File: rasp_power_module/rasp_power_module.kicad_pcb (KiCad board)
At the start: 2 copper layers, 45.7 x 59.3 mm, 22 parts, among them J1 Conn_01x02, J2 Conn_01x05, J3 Conn_01x02, J5 Conn_01x02, J7 Conn_01x02, J8 Conn_01x02, J9 Conn_01x02, K1 G5V-1, K2 FINDER-36.11, Q1 S8050 J3Y

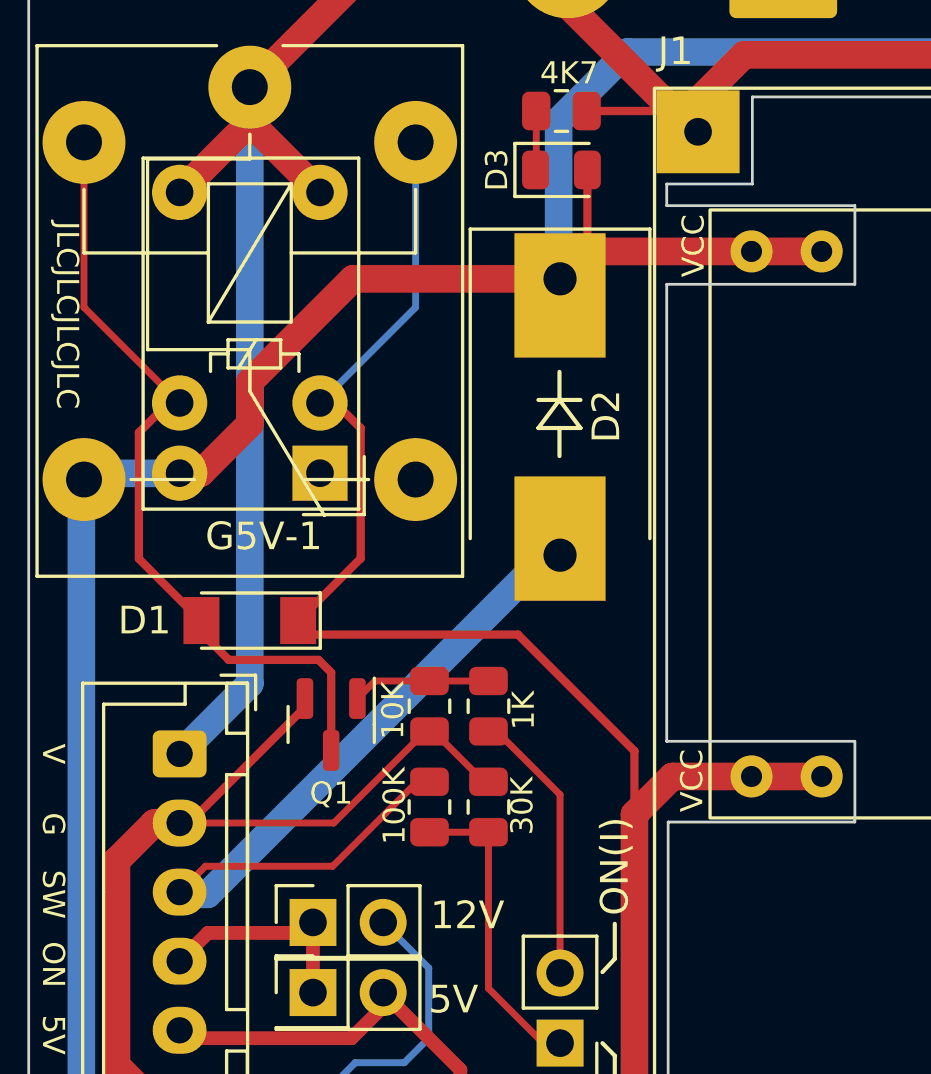
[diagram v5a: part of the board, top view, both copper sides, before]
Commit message: rasp_pm 다이오드 부품 교체
Signed-off-by: Ju, Gyeong-min <jcmh74@gmail.com>
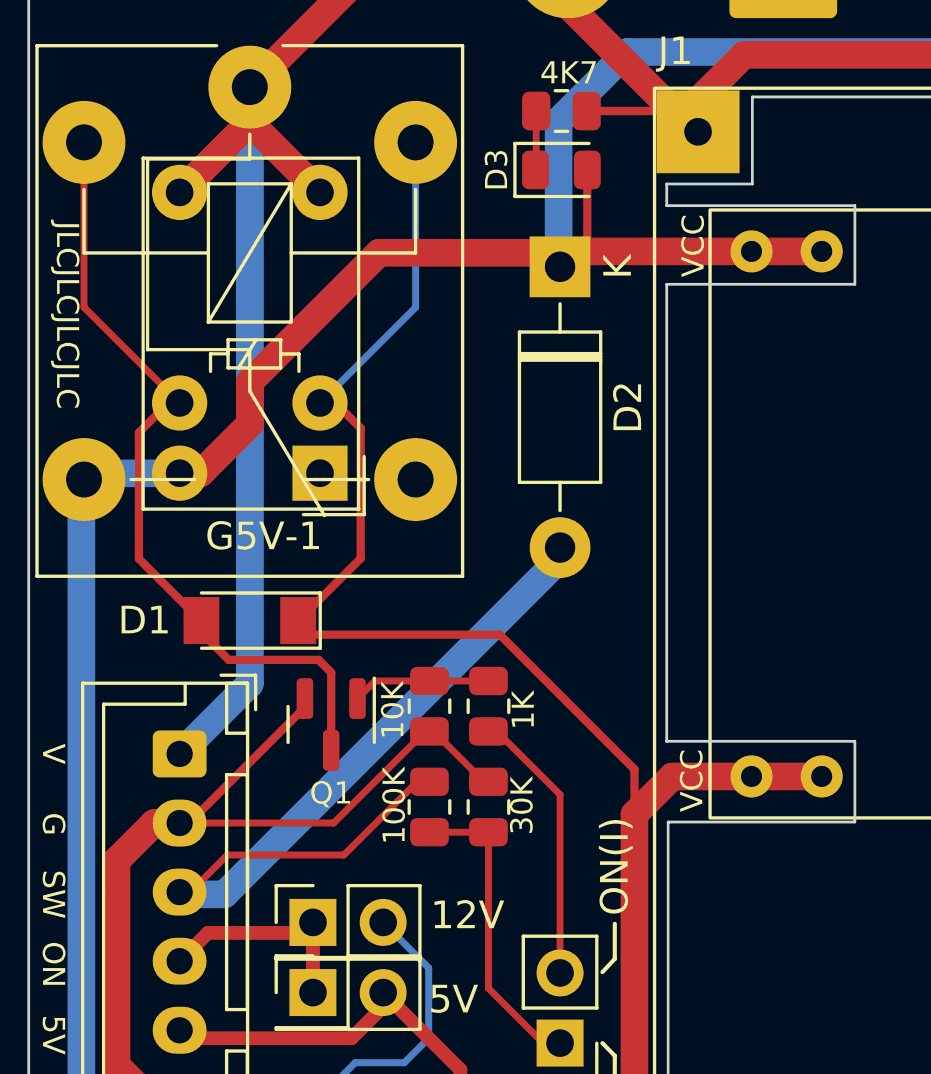
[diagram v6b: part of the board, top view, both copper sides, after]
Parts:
- D1: value ZMM5V6-M -> LL4148
- D2: value 1N4001 -> 1N4007; footprint Diode_SMD:D_SMC-RM10_Universal_Handsoldering -> Diode_THT:D_DO-41_SOD81_P10.16mm_Horizontal
- moved D2 5.44 mm to (141.0, 72.5)
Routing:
- net /SWITCH: track 29.8 -> 30.4 mm

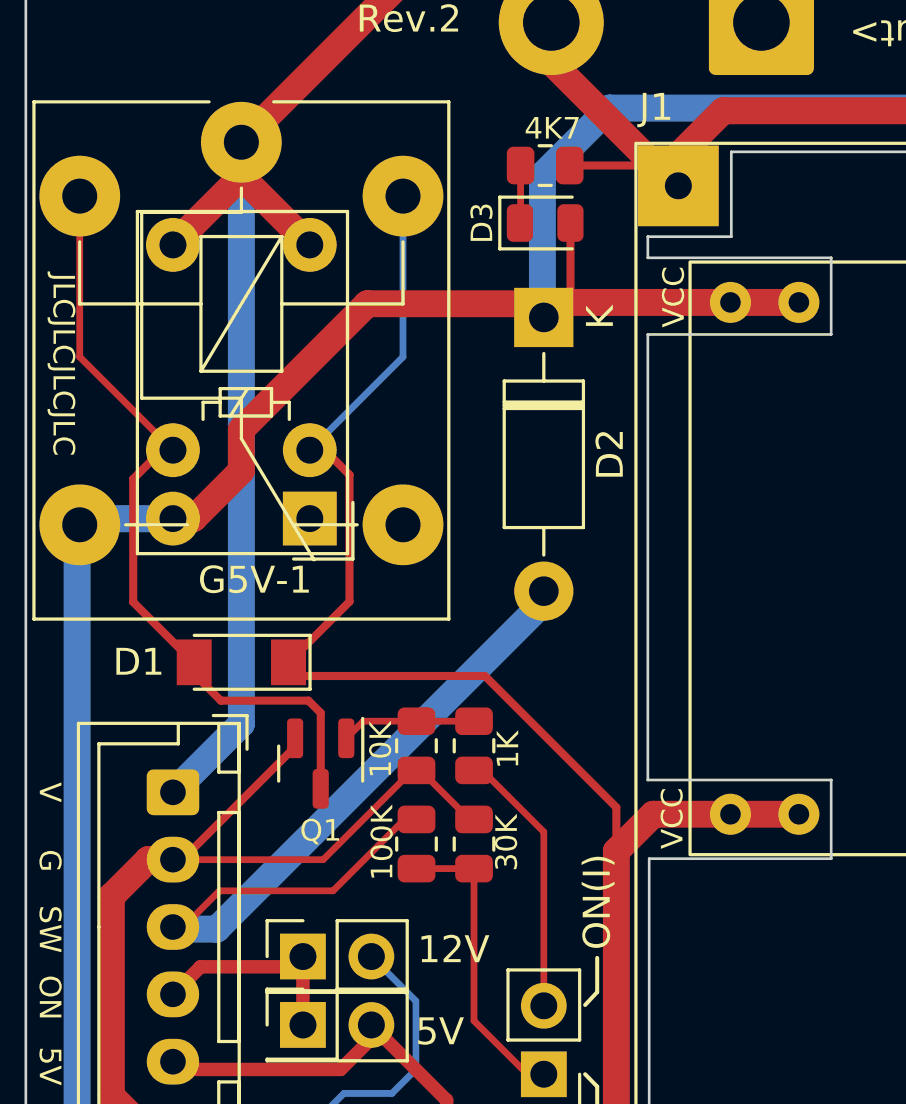
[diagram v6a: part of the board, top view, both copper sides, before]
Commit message: rasp_pi 다이오드 교체
Signed-off-by: Ju, Gyeong-min <jcmh74@gmail.com>
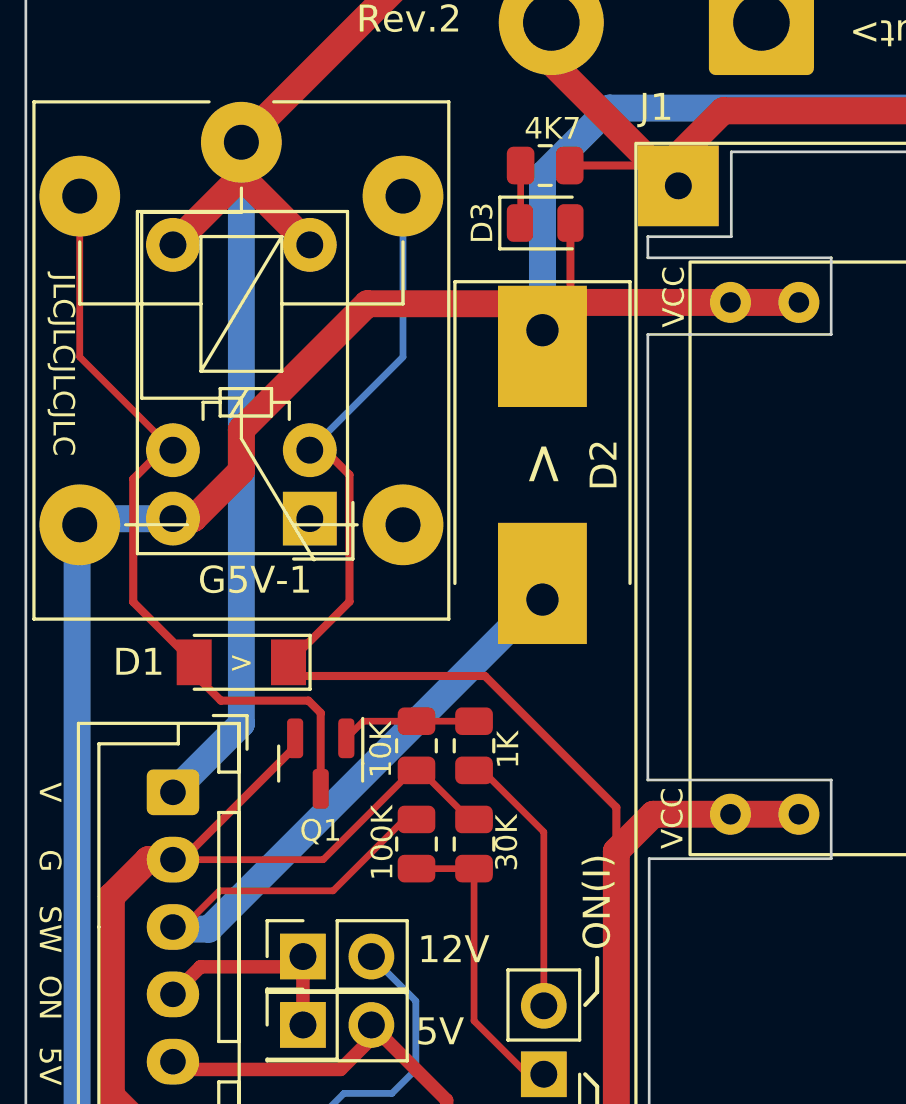
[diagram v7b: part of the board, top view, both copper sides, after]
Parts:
- D2: footprint Diode_THT:D_DO-41_SOD81_P10.16mm_Horizontal -> Diode_SMD:D_SMC-RM10_Universal_Handsoldering
- moved D2 5.47 mm to (141.0, 78.0)
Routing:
- net 12V_ON: track 113.3 -> 114.3 mm
- net /SWITCH: track 30.4 -> 29.8 mm
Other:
- board text added: ">"

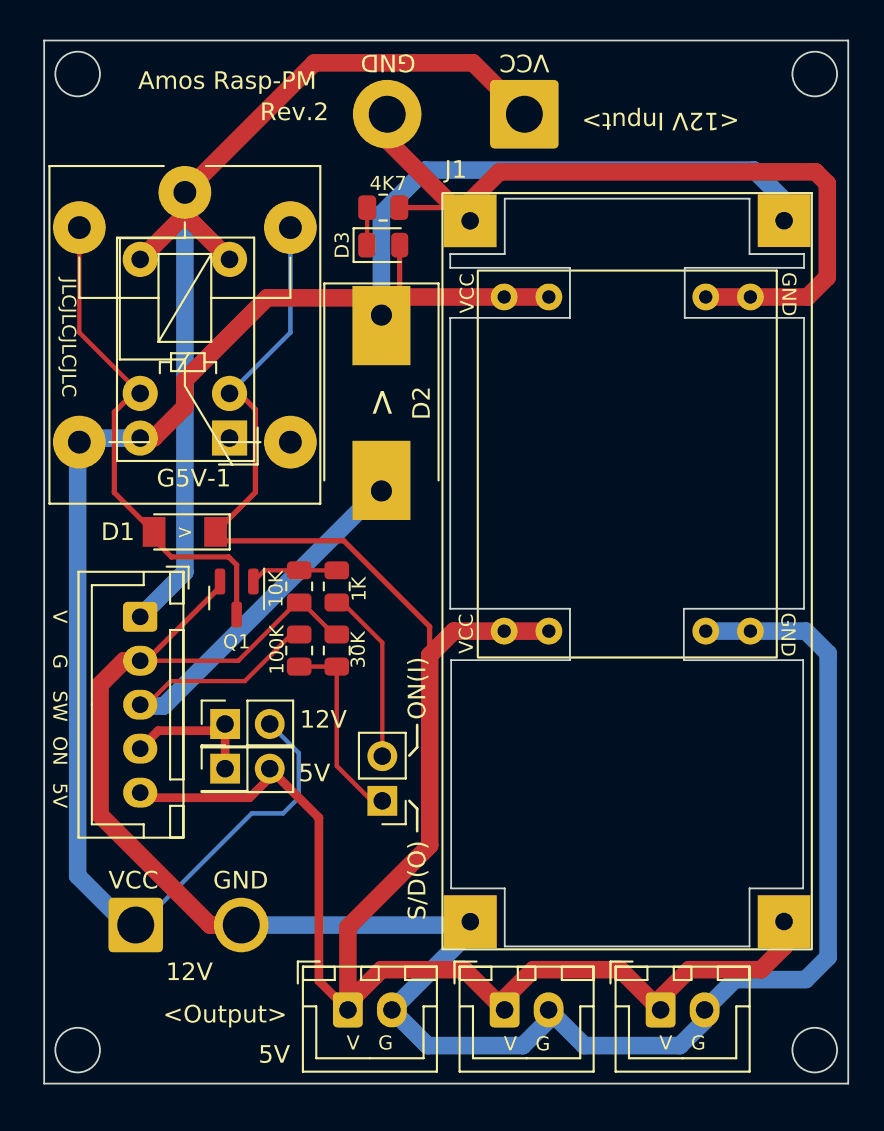
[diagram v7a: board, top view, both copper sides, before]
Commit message: rasp_pm 릴레이 종류 변경
Signed-off-by: Ju, Gyeong-min <jcmh74@gmail.com>
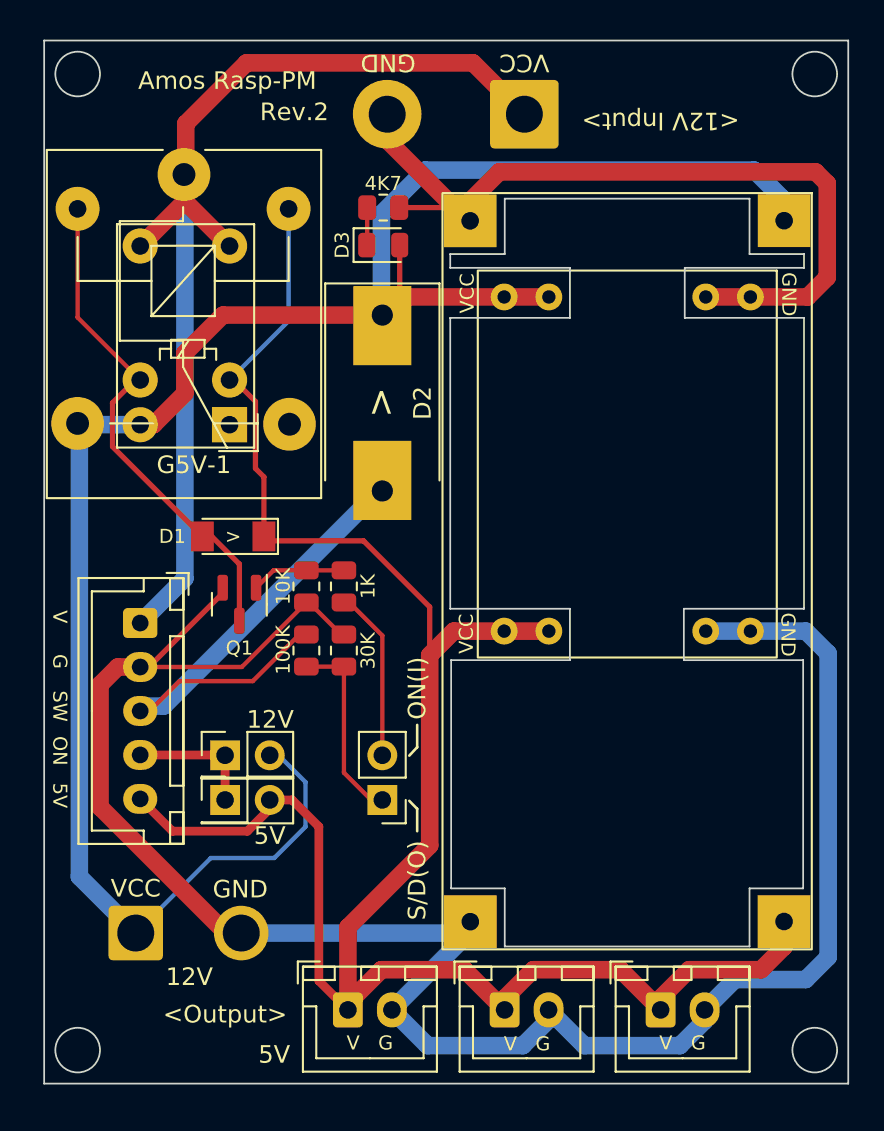
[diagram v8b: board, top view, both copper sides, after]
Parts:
- K2: value FINDER-36.11 -> SANYOU_SRD_Form_C; footprint Relay_THT:Relay_SPDT_Finder_36.11 -> Relay_THT:Relay_SPDT_SANYOU_SRD_Series_Form_C
- moved D1 2.75 mm to (132.5, 85.6)
- moved JP2 1.78 mm to (132.1, 100.6)
- moved JP1 1.78 mm to (132.1, 98.0)
- moved K2 1.02 mm to (129.7, 65.0)
- moved K1 0.76 mm to (132.3, 79.2)
- moved J5 0.46 mm to (127.0, 108.2)
- moved R2 0.41 mm to (136.7, 88.4)
- moved R3 0.41 mm to (136.7, 92.1)
- moved R1 0.41 mm to (138.8, 88.4)
- moved R4 0.41 mm to (138.8, 92.1)
- moved Q1 0.39 mm to (132.9, 89.5)
- moved J2 0.36 mm to (127.3, 90.5)
- moved D2 0.05 mm to (141.0, 78.0)
- moved J3 0.05 mm to (141.0, 100.6)
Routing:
- net Relay_In: track 57.2 -> 60.6 mm
- net 5V_ON: track 122.2 -> 120.0 mm
- net InGND: track 162.9 -> 163.6 mm
- net /POWER_SIG: track 10.4 -> 9.77 mm
- net /ON_LED: track 7.95 -> 7.37 mm
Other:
- board text removed: "JLCJLCJLCJLC"
